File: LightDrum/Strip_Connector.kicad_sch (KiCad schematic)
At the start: 1 part, among them J1 LED D-SUB

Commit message: General component placement
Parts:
- renumbered J1 to J601
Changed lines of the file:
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@@
   (symbol (lib_id "power:VCC") (at 20.32 107.95 0) (unit 1)
     (in_bom yes) (on_board yes)
-    (property "Reference" "#PWR033" (id 0) (at 20.32 111.76 0)
+    (property "Reference" "#PWR0601" (id 0) (at 20.32 111.76 0)
       (effects (font (size 1.27 1.27)) hide)
     )
@@
   (symbol (lib_id "Connector:DB37_Female_MountingHoles") (at 48.26 71.12 0) (unit 1)
     (in_bom yes) (on_board yes) (fields_autoplaced)
-    (property "Reference" "J1" (id 0) (at 53.34 69.8499 0)
+    (property "Reference" "J601" (id 0) (at 53.34 69.8499 0)
       (effects (font (size 1.27 1.27)) (justify left))
     )
@@
   (symbol (lib_id "power:GND") (at 48.26 124.46 0) (unit 1)
     (in_bom yes) (on_board yes)
-    (property "Reference" "#PWR034" (id 0) (at 48.26 130.81 0)
+    (property "Reference" "#PWR0602" (id 0) (at 48.26 130.81 0)
       (effects (font (size 1.27 1.27)) hide)
     )

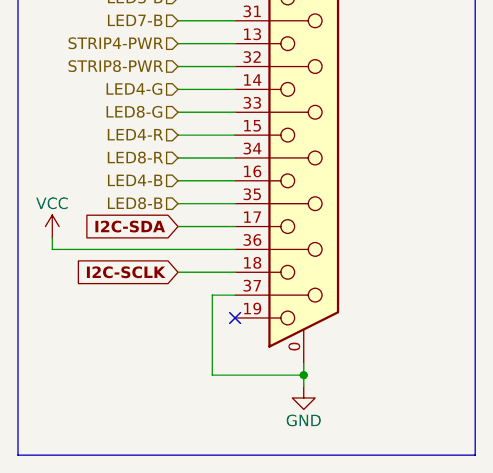
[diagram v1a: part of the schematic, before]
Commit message: Simplify analog power supply and add some routing
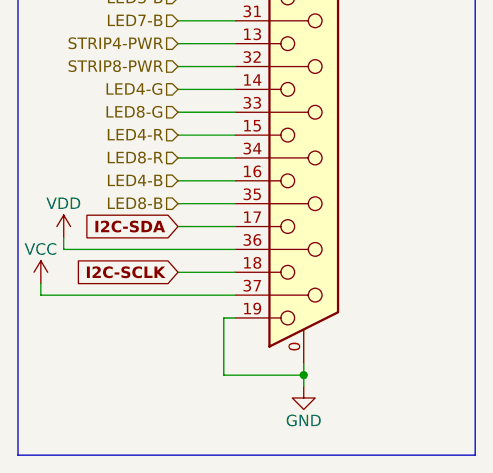
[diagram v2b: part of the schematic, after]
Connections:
- net GND: now also J601.19; no longer J601.37
- net VCC: now also J601.37; no longer J601.36
- new net VDD: J601.36
- no-connect marks 1 -> 0
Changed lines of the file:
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@@
   (junction (at 48.26 123.19) (diameter 0) (color 0 0 0 0)
   )
-  (no_connect (at 40.64 116.84))
+  (wire (pts (xy 19.05 113.03) (xy 19.05 114.3))
+    (stroke (width 0) (type default) (color 0 0 0 0))
+  )
   (wire (pts (xy 34.29 27.94) (xy 40.64 27.94))
     (stroke (width 0) (type default) (color 0 0 0 0))
   )
+  (wire (pts (xy 39.37 116.84) (xy 39.37 123.19))
+    (stroke (width 0) (type default) (color 0 0 0 0))
+  )
   (wire (pts (xy 34.29 35.56) (xy 40.64 35.56))
     (stroke (width 0) (type default) (color 0 0 0 0))
@@
     (stroke (width 0) (type default) (color 0 0 0 0))
   )
-  (wire (pts (xy 38.1 123.19) (xy 38.1 114.3))
-    (stroke (width 0) (type default) (color 0 0 0 0))
-  )
   (wire (pts (xy 34.29 40.64) (xy 40.64 40.64))
     (stroke (width 0) (type default) (color 0 0 0 0))
@@
     (stroke (width 0) (type default) (color 0 0 0 0))
   )
+  (wire (pts (xy 39.37 116.84) (xy 40.64 116.84))
+    (stroke (width 0) (type default) (color 0 0 0 0))
+  )
   (wire (pts (xy 48.26 121.92) (xy 48.26 123.19))
     (stroke (width 0) (type default) (color 0 0 0 0))
@@
     (stroke (width 0) (type default) (color 0 0 0 0))
   )
+  (wire (pts (xy 40.64 114.3) (xy 19.05 114.3))
+    (stroke (width 0) (type default) (color 0 0 0 0))
+  )
+  (wire (pts (xy 39.37 123.19) (xy 48.26 123.19))
+    (stroke (width 0) (type default) (color 0 0 0 0))
+  )
   (wire (pts (xy 34.29 101.6) (xy 40.64 101.6))
     (stroke (width 0) (type default) (color 0 0 0 0))
@@
     (stroke (width 0) (type default) (color 0 0 0 0))
   )
-  (wire (pts (xy 38.1 114.3) (xy 40.64 114.3))
-    (stroke (width 0) (type default) (color 0 0 0 0))
-  )
   (wire (pts (xy 34.29 30.48) (xy 40.64 30.48))
     (stroke (width 0) (type default) (color 0 0 0 0))
   )
-  (wire (pts (xy 48.26 123.19) (xy 38.1 123.19))
-    (stroke (width 0) (type default) (color 0 0 0 0))
-  )
   (wire (pts (xy 34.29 99.06) (xy 40.64 99.06))
     (stroke (width 0) (type default) (color 0 0 0 0))
@@
     (stroke (width 0) (type default) (color 0 0 0 0))
   )
-  (wire (pts (xy 20.32 107.95) (xy 20.32 109.22))
-    (stroke (width 0) (type default) (color 0 0 0 0))
-  )
-  (wire (pts (xy 20.32 109.22) (xy 40.64 109.22))
+  (wire (pts (xy 21.59 107.95) (xy 21.59 109.22))
+    (stroke (width 0) (type default) (color 0 0 0 0))
+  )
+  (wire (pts (xy 21.59 109.22) (xy 40.64 109.22))
     (stroke (width 0) (type default) (color 0 0 0 0))
   )
@@
   (hierarchical_label "STRIP3-PWR" (shape input) (at 34.29 66.04 180)
     (effects (font (size 1.27 1.27)) (justify right))
-  )
-  (symbol (lib_id "power:VCC") (at 20.32 107.95 0) (unit 1)
-    (in_bom yes) (on_board yes)
-    (property "Reference" "#PWR0601" (id 0) (at 20.32 111.76 0)
-      (effects (font (size 1.27 1.27)) hide)
-    )
-    (property "Value" "VCC" (id 1) (at 20.32 104.14 0))
-    (property "Footprint" "" (id 2) (at 20.32 107.95 0)
-      (effects (font (size 1.27 1.27)) hide)
-    )
-    (property "Datasheet" "" (id 3) (at 20.32 107.95 0)
-      (effects (font (size 1.27 1.27)) hide)
-    )
-    (pin "1")
   )
   (symbol (lib_id "Connector:DB37_Female_MountingHoles") (at 48.26 71.12 0) (unit 1)
@@
       (effects (font (size 1.27 1.27)) hide)
     )
+    (pin "1")
+  )
+  (symbol (lib_id "power:VDD") (at 21.59 107.95 0) (unit 1)
+    (in_bom yes) (on_board yes)
+    (property "Reference" "#PWR0131" (id 0) (at 21.59 111.76 0)
+      (effects (font (size 1.27 1.27)) hide)
+    )
+    (property "Value" "VDD" (id 1) (at 21.59 104.14 0))
+    (property "Footprint" "" (id 2) (at 21.59 107.95 0)
+      (effects (font (size 1.27 1.27)) hide)
+    )
+    (property "Datasheet" "" (id 3) (at 21.59 107.95 0)
+      (effects (font (size 1.27 1.27)) hide)
+    )
+    (pin "1")
+  )
+  (symbol (lib_id "power:VCC") (at 19.05 113.03 0) (unit 1)
+    (in_bom yes) (on_board yes)
+    (property "Reference" "#PWR0132" (id 0) (at 19.05 116.84 0)
+      (effects (font (size 1.27 1.27)) hide)
+    )
+    (property "Value" "VCC" (id 1) (at 19.05 109.22 0))
+    (property "Footprint" "" (id 2) (at 19.05 113.03 0)
+      (effects (font (size 1.27 1.27)) hide)
+    )
+    (property "Datasheet" "" (id 3) (at 19.05 113.03 0)
+      (effects (font (size 1.27 1.27)) hide)
+    )

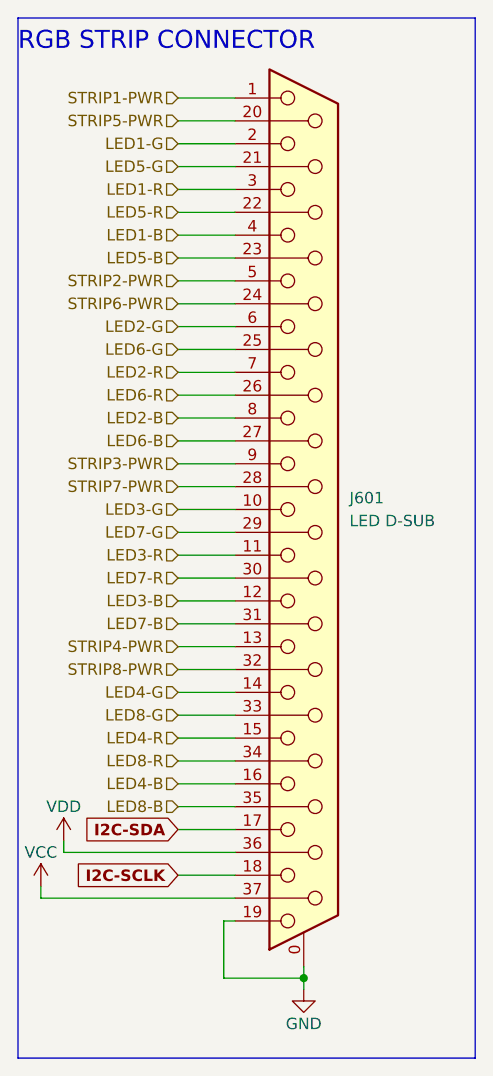
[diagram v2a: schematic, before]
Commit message: Replace barrel jacks with proper DIN4 conn and more
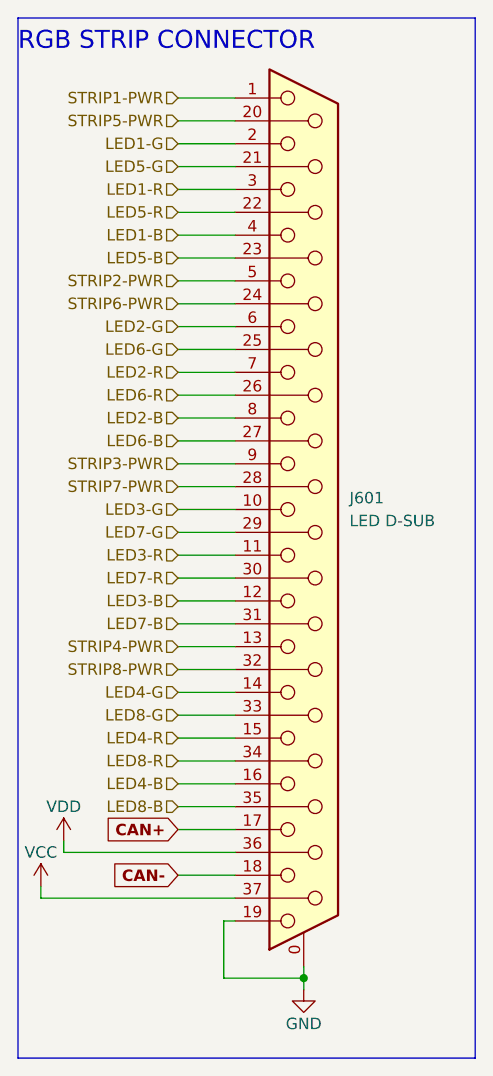
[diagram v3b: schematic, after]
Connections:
- net I2C-SCLK renamed CAN-
- net I2C-SDA renamed CAN+
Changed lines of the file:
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@@
     (effects (font (size 2 2)) (justify left bottom))
   )
-  (global_label "I2C-SCLK" (shape input) (at 34.29 111.76 180) (fields_autoplaced)
+  (global_label "CAN-" (shape input) (at 34.29 111.76 180) (fields_autoplaced)
     (effects (font (size 1.27 1.27) (thickness 0.254) bold) (justify right))
-    (property "Intersheet References" "${INTERSHEET_REFS}" (id 0) (at 22.2522 111.633 0)
+    (property "Intersheet References" "${INTERSHEET_REFS}" (id 0) (at 26.4251 111.633 0)
       (effects (font (size 1.27 1.27) (thickness 0.254) bold) (justify right) hide)
     )
   )
-  (global_label "I2C-SDA" (shape input) (at 34.29 106.68 180) (fields_autoplaced)
+  (global_label "CAN+" (shape input) (at 34.29 106.68 180) (fields_autoplaced)
     (effects (font (size 1.27 1.27) (thickness 0.254) bold) (justify right))
-    (property "Intersheet References" "${INTERSHEET_REFS}" (id 0) (at 23.4617 106.553 0)
+    (property "Intersheet References" "${INTERSHEET_REFS}" (id 0) (at 26.4251 106.553 0)
       (effects (font (size 1.27 1.27) (thickness 0.254) bold) (justify right) hide)
     )

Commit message: interface layout completed - REV6
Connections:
- net GND: now also J601.36; no longer J601.19
- net VDD: now also J601.19; no longer J601.36
- net CAN+ renamed DMX-
- net CAN- renamed DMX+
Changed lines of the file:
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@@
   (junction (at 48.26 123.19) (diameter 0) (color 0 0 0 0)
   )
-  (wire (pts (xy 19.05 113.03) (xy 19.05 114.3))
+  (wire (pts (xy 24.13 111.76) (xy 24.13 114.3))
     (stroke (width 0) (type default) (color 0 0 0 0))
   )
@@
     (stroke (width 0) (type default) (color 0 0 0 0))
   )
-  (wire (pts (xy 39.37 116.84) (xy 39.37 123.19))
+  (wire (pts (xy 19.05 116.84) (xy 40.64 116.84))
+    (stroke (width 0) (type default) (color 0 0 0 0))
+  )
+  (wire (pts (xy 38.1 109.22) (xy 38.1 123.19))
     (stroke (width 0) (type default) (color 0 0 0 0))
   )
@@
     (stroke (width 0) (type default) (color 0 0 0 0))
   )
-  (wire (pts (xy 39.37 116.84) (xy 40.64 116.84))
+  (wire (pts (xy 38.1 109.22) (xy 40.64 109.22))
     (stroke (width 0) (type default) (color 0 0 0 0))
   )
@@
     (stroke (width 0) (type default) (color 0 0 0 0))
   )
-  (wire (pts (xy 40.64 114.3) (xy 19.05 114.3))
-    (stroke (width 0) (type default) (color 0 0 0 0))
-  )
-  (wire (pts (xy 39.37 123.19) (xy 48.26 123.19))
+  (wire (pts (xy 40.64 114.3) (xy 24.13 114.3))
+    (stroke (width 0) (type default) (color 0 0 0 0))
+  )
+  (wire (pts (xy 38.1 123.19) (xy 48.26 123.19))
     (stroke (width 0) (type default) (color 0 0 0 0))
   )
@@
     (stroke (width 0) (type default) (color 0 0 0 0))
   )
-  (wire (pts (xy 21.59 107.95) (xy 21.59 109.22))
-    (stroke (width 0) (type default) (color 0 0 0 0))
-  )
-  (wire (pts (xy 21.59 109.22) (xy 40.64 109.22))
+  (wire (pts (xy 19.05 111.76) (xy 19.05 116.84))
     (stroke (width 0) (type default) (color 0 0 0 0))
   )
@@
     (effects (font (size 2 2)) (justify left bottom))
   )
-  (global_label "CAN-" (shape input) (at 34.29 111.76 180) (fields_autoplaced)
-    (effects (font (size 1.27 1.27) (thickness 0.254) bold) (justify right))
-    (property "Intersheet References" "${INTERSHEET_REFS}" (id 0) (at 26.4251 111.633 0)
-      (effects (font (size 1.27 1.27) (thickness 0.254) bold) (justify right) hide)
-    )
-  )
-  (global_label "CAN+" (shape input) (at 34.29 106.68 180) (fields_autoplaced)
-    (effects (font (size 1.27 1.27) (thickness 0.254) bold) (justify right))
-    (property "Intersheet References" "${INTERSHEET_REFS}" (id 0) (at 26.4251 106.553 0)
-      (effects (font (size 1.27 1.27) (thickness 0.254) bold) (justify right) hide)
-    )
-  )
   (hierarchical_label "STRIP2-PWR" (shape input) (at 34.29 45.72 180)
     (effects (font (size 1.27 1.27)) (justify right))
@@
     (effects (font (size 1.27 1.27)) (justify right))
   )
+  (hierarchical_label "DMX+" (shape bidirectional) (at 34.29 111.76 180)
+    (effects (font (size 1.27 1.27)) (justify right))
+  )
   (hierarchical_label "LED1-G" (shape input) (at 34.29 30.48 180)
     (effects (font (size 1.27 1.27)) (justify right))
@@
   )
   (hierarchical_label "STRIP7-PWR" (shape input) (at 34.29 68.58 180)
+    (effects (font (size 1.27 1.27)) (justify right))
+  )
+  (hierarchical_label "DMX-" (shape bidirectional) (at 34.29 106.68 180)
     (effects (font (size 1.27 1.27)) (justify right))
   )
@@
     (pin "1")
   )
-  (symbol (lib_id "power:VDD") (at 21.59 107.95 0) (unit 1)
+  (symbol (lib_id "power:VDD") (at 19.05 111.76 0) (unit 1)
     (in_bom yes) (on_board yes)
-    (property "Reference" "#PWR0131" (id 0) (at 21.59 111.76 0)
-      (effects (font (size 1.27 1.27)) hide)
-    )
-    (property "Value" "VDD" (id 1) (at 21.59 104.14 0))
-    (property "Footprint" "" (id 2) (at 21.59 107.95 0)
-      (effects (font (size 1.27 1.27)) hide)
-    )
-    (property "Datasheet" "" (id 3) (at 21.59 107.95 0)
+    (property "Reference" "#PWR0131" (id 0) (at 19.05 115.57 0)
+      (effects (font (size 1.27 1.27)) hide)
+    )
+    (property "Value" "VDD" (id 1) (at 19.05 107.95 0))
+    (property "Footprint" "" (id 2) (at 19.05 111.76 0)
+      (effects (font (size 1.27 1.27)) hide)
+    )
+    (property "Datasheet" "" (id 3) (at 19.05 111.76 0)
       (effects (font (size 1.27 1.27)) hide)
     )
     (pin "1")
   )
-  (symbol (lib_id "power:VCC") (at 19.05 113.03 0) (unit 1)
+  (symbol (lib_id "power:VCC") (at 24.13 111.76 0) (unit 1)
     (in_bom yes) (on_board yes)
-    (property "Reference" "#PWR0132" (id 0) (at 19.05 116.84 0)
-      (effects (font (size 1.27 1.27)) hide)
-    )
-    (property "Value" "VCC" (id 1) (at 19.05 109.22 0))
-    (property "Footprint" "" (id 2) (at 19.05 113.03 0)
-      (effects (font (size 1.27 1.27)) hide)
-    )
-    (property "Datasheet" "" (id 3) (at 19.05 113.03 0)
-      (effects (font (size 1.27 1.27)) hide)
-    )
+    (property "Reference" "#PWR0132" (id 0) (at 24.13 115.57 0)
+      (effects (font (size 1.27 1.27)) hide)
+    )
+    (property "Value" "VCC" (id 1) (at 24.13 107.95 0))
+    (property "Footprint" "" (id 2) (at 24.13 111.76 0)
+      (effects (font (size 1.27 1.27)) hide)
+    )
+    (property "Datasheet" "" (id 3) (at 24.13 111.76 0)
+      (effects (font (size 1.27 1.27)) hide)
+    )

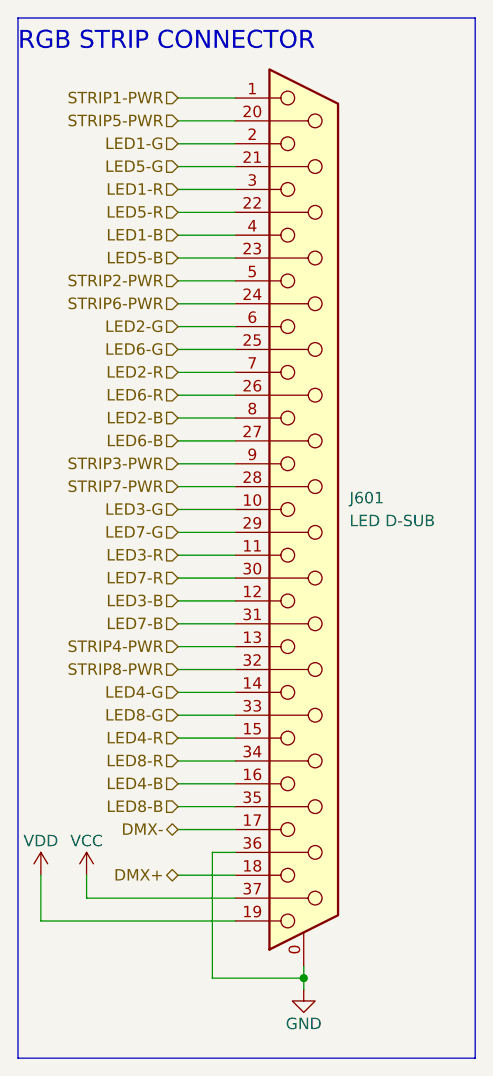
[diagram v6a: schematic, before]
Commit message: Add main page to sch and xlr audio input diff-amp
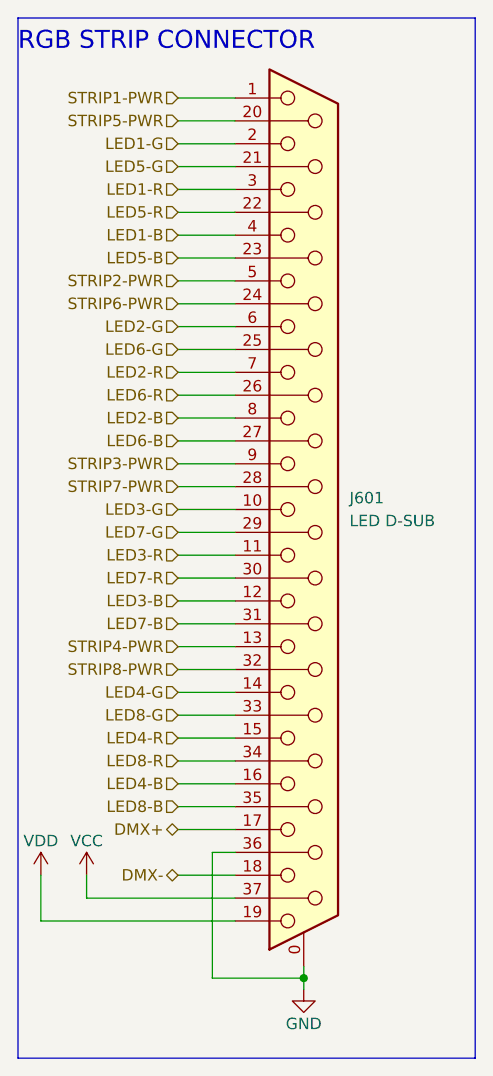
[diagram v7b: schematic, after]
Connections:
- net DMX+: now also J601.17; no longer J601.18
- net DMX-: now also J601.18; no longer J601.17
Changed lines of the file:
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@@
     (effects (font (size 1.27 1.27)) (justify right))
   )
-  (hierarchical_label "DMX+" (shape bidirectional) (at 34.29 111.76 180)
+  (hierarchical_label "DMX+" (shape bidirectional) (at 34.29 106.68 180)
     (effects (font (size 1.27 1.27)) (justify right))
   )
@@
     (effects (font (size 1.27 1.27)) (justify right))
   )
-  (hierarchical_label "DMX-" (shape bidirectional) (at 34.29 106.68 180)
+  (hierarchical_label "DMX-" (shape bidirectional) (at 34.29 111.76 180)
     (effects (font (size 1.27 1.27)) (justify right))
   )
